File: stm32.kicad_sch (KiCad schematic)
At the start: 71 parts, among them J4 Conn_ST_STDC14, J5 Conn_02x20_Odd_Even, J7 TC2030 - TAG Connect, Q5 SI2301CDS-T1-GE3, SW1 SW_Push, SW2 SW_Push, U3 STM32F427V_G-I_Tx, X1 8MHz 20pF

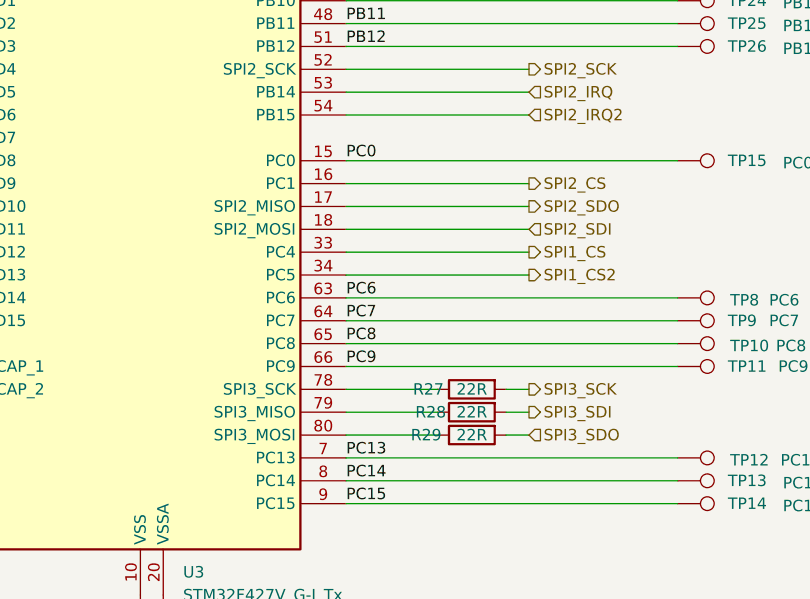
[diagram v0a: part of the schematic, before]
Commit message: remove tp and rotate cpu
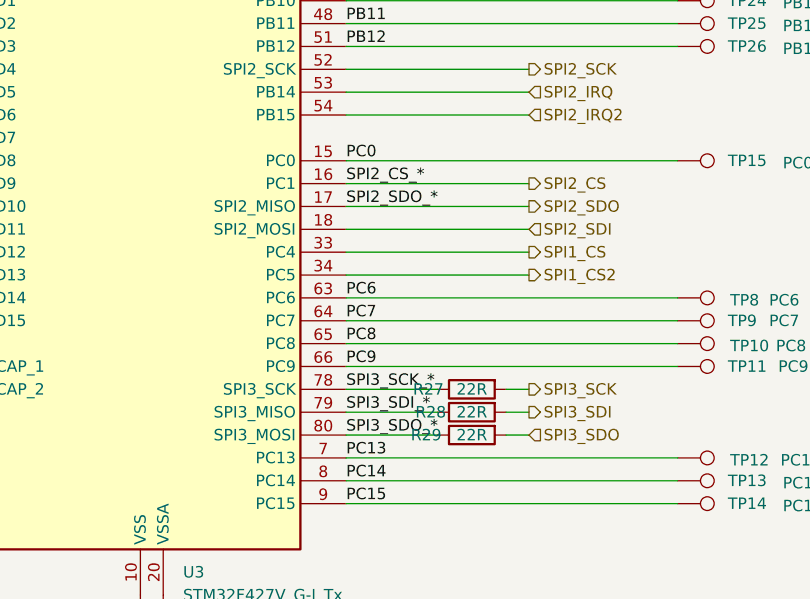
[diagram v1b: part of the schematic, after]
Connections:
- net SPI3_SDI_*: now reaches R28.1, U3.79 (PC11)
- net SPI3_SDO_*: now reaches R29.1, U3.80 (PC12)
- net SPI3_SCK_*: now reaches R27.1, U3.78 (PC10)
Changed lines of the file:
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@@
+		)
+	)
+	(label "SPI3_SDO_*"
+		(at 186.69 212.09 0)
+		(effects
+			(font
+				(size 1.27 1.27)
+			)
+			(justify left bottom)
 		)
 	)
@@
 		)
 	)
+	(label "SPI3_SCK_*"
+		(at 186.69 207.01 0)
+		(effects
+			(font
+				(size 1.27 1.27)
+			)
+			(justify left bottom)
+		)
+	)
 	(label "PE10"
 		(at 269.24 256.54 0)
@@
 		)
 	)
+	(label "SPI3_SDI_*"
+		(at 186.69 209.55 0)
+		(effects
+			(font
+				(size 1.27 1.27)
+			)
+			(justify left bottom)
+		)
+	)
 	(label "PD7"
 		(at 256.54 248.92 180)
@@
 		)
 	)
+	(label "SPI2_CS_*"
+		(at 186.69 184.15 0)
+		(effects
+			(font
+				(size 1.27 1.27)
+			)
+			(justify left bottom)
+		)
+	)
 	(label "PE11"
 		(at 140.97 146.05 180)
@@
 		)
 	)
+	(label "SPI2_SDO_*"
+		(at 186.69 186.69 0)
+		(effects
+			(font
+				(size 1.27 1.27)
+			)
+			(justify left bottom)
+		)
+	)

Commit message: pre JLCPCB try 1
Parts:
- C11, C15, C16, C17, C30, C9: LCSC (none) -> C14663
- C12: LCSC C1525 -> C14663; Manufacturer Samsung -> (none)
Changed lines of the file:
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@@
 	(label "SPI3_SDO_*"
 		(at 186.69 212.09 0)
+		(fields_autoplaced yes)
 		(effects
 			(font
@@
 	(label "SPI3_SCK_*"
 		(at 186.69 207.01 0)
+		(fields_autoplaced yes)
 		(effects
 			(font
@@
 	(label "SPI3_SDI_*"
 		(at 186.69 209.55 0)
+		(fields_autoplaced yes)
 		(effects
 			(font
@@
 	(label "SPI2_CS_*"
 		(at 186.69 184.15 0)
+		(fields_autoplaced yes)
 		(effects
 			(font
@@
 	(label "SPI2_SDO_*"
 		(at 186.69 186.69 0)
+		(fields_autoplaced yes)
 		(effects
 			(font
@@
 			)
 		)
-		(property "LCSC" ""
+		(property "LCSC" "C14663"
 			(at 158.75 67.31 0)
 			(effects
@@
 			)
 		)
-		(property "LCSC" ""
+		(property "LCSC" "C14663"
 			(at 161.29 67.31 0)
 			(effects
@@
 			)
 		)
-		(property "LCSC" ""
+		(property "LCSC" "C14663"
 			(at 168.91 67.31 0)
 			(effects
@@
 			)
 		)
-		(property "LCSC" "C1525"
+		(property "LCSC" "C14663"
 			(at 163.83 67.31 0)
 			(effects
@@
 			)
 		)
-		(property "Manufacturer" "Samsung"
+		(property "Manufacturer" ""
 			(at 163.83 67.31 0)
 			(effects
@@
 			)
 		)
-		(property "LCSC" ""
+		(property "LCSC" "C14663"
 			(at 171.45 67.31 0)
 			(effects
@@
 			)
 		)
-		(property "LCSC" ""
+		(property "LCSC" "C14663"
 			(at 149.86 58.42 0)
 			(effects
@@
 			)
 		)
-		(property "LCSC" ""
+		(property "LCSC" "C14663"
 			(at 166.37 67.31 0)
 			(effects

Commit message: STM32 C117815
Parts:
- U3: LCSC (none) -> C117815
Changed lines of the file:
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@@
 			)
 		)
-		(property "LCSC" ""
+		(property "LCSC" "C117815"
 			(at 163.83 158.75 0)
 			(effects

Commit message: SENT TO jlcpcb
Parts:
- D11, D4, D5, D6: JLCPCB Rotation Offset (none) -> 180
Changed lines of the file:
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@@
+			)
+		)
+		(property "JLCPCB Rotation Offset" "180"
+			(at 314.96 105.41 0)
+			(effects
+				(font
+					(size 1.27 1.27)
+				)
+				(hide yes)
 			)
 		)
@@
 			)
 		)
+		(property "JLCPCB Rotation Offset" "180"
+			(at 314.96 113.03 0)
+			(effects
+				(font
+					(size 1.27 1.27)
+				)
+				(hide yes)
+			)
+		)
 		(pin "1"
 		)
@@
 			)
 		)
+		(property "JLCPCB Rotation Offset" "180"
+			(at 314.96 107.95 0)
+			(effects
+				(font
+					(size 1.27 1.27)
+				)
+				(hide yes)
+			)
+		)
 		(pin "1"
 		)
@@
 			(at 314.96 110.49 0)
 			(effects
+				(font
+					(size 1.27 1.27)
+				)
+				(hide yes)
+			)
+		)
+		(property "JLCPCB Rotation Offset" "180"
+			(at 314.96 110.49 0)
+			(effects

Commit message: version 2 changes
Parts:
- added R6: 100R, Resistor_SMD:R_0603_1608Metric, symbol Device:R
- FB1: symbol l8-kicad-rescue:Ferrite_Bead-Device -> Device:FerriteBead
- J4: footprint dnt:CON14_2X7_DUK_FTSH_SAI -> dnt:SAMTEC_FTSH-107-01-F-DV-K-Fix
- J7: value TC2030 - TAG Connect -> TC2070 - TAG Connect; footprint Connector:Tag-Connect_TC2030-IDC-NL_2x03_P1.27mm_Vertical -> Connector:Tag-Connect_TC2070-IDC-FP_2x07_P1.27mm_Vertical; symbol l8-kicad-rescue:Conn_01x06_Male-Connector -> Connector:Conn_ST_STDC14; now in the parts list
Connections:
- net +3.3V: now also J7.3 (VCC); no longer J7.1 (Pin_1)
- net GND: now also J7.7 (GND), R6.2
- net NRST: now also J7.12 (~{RST}); no longer J7.3 (Pin_3)
- net SYS_JTCK-SWCLK: now also J7.6 (JCLK/SWCLK); no longer J7.4 (Pin_4)
- net SYS_JTDI: now also J7.10 (JTDI/NC)
- net SYS_JTDO-SWO: now also J7.8 (JTDO/SWO); no longer J7.6 (Pin_6)
- net SYS_JTMS-SWDIO: now also J7.4 (JTMS/SWDIO); no longer J7.2 (Pin_2)
- net USART2_RX: now also J7.13 (VCP_RX)
- net USART2_TX: now also J7.14 (VCP_TX)
- net SPI3_CS renamed SPI4_CS_2
- net SPI4_CS renamed SPI4_CS_1
- new net: J7.11 (GNDDetect), R6.1
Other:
- moved on the sheet: C13, C14, D11, D4, D5, D6, J4, R35, RN2, X1

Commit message: x
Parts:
- removed Q5: SI2301CDS-T1-GE3, Package_TO_SOT_SMD:SOT-23, symbol dnt:SI2301CDS-T1-GE3
- removed R27, R28, R29: 22R, Resistor_SMD:R_0603_1608Metric, symbol Device:R
- added Q3: AO3400A, Package_TO_SOT_SMD:SOT-23, symbol dnt:AO3400A
- D11, D4, D5, D6: footprint LED_SMD:LED_0603_1608Metric -> dnt:LED_0603_1608Metric - polarity
- FB1: value ~ -> 4.7uH
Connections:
- net GND: now also Q3.2 (S)
- net at BZ1.2 (-): now also Q3.3 (D)
- net at R32.1, R33.2: now also Q3.1 (G)
- no-connect marks 1 -> 4

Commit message: version 2 initial
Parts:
- removed C29: 10nF, Capacitor_SMD:C_0603_1608Metric, symbol Device:C
- removed TP16: PA0, dnt:TestPoint_Pad_D1.0mm FP .6R, symbol Connector:TestPoint
- added C26: 10uF, Capacitor_SMD:C_0805_2012Metric, symbol Device:C
- J4, J7: now not fitted
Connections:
- net +3.3V: now also C26.2
- net GND: now also C26.1
- net SPI2_SDI: now also U3.17 (PC2); no longer U3.18 (PC3)
- net SPI2_SDO: now also U3.18 (PC3); no longer U3.17 (PC2)
- net PA0 renamed SYS_WAKEUP
- net SPI3_SCK_* renamed SPI3_SCK
- net SPI3_SDI_* renamed SPI3_SDI
- net SPI3_SDO_* renamed SPI3_SDO
- removed net SYS_JTDI: J4.10 (JTDI/NC), J7.10 (JTDI/NC), U3.77 (PA15)
- new net SPI3_CS: U3.77 (PA15)
- no-connect marks 4 -> 7
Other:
- note added: "SPI1 40MHZ SPI2 20MHz SPI3 20MHz SPI4 40MHz"
- moved on the sheet: C1, C11, C12, C15, C16, C17, C23, C30, C8, C9, FB1
